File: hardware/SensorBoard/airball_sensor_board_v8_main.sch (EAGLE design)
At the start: 56 parts, among them IC1 CP2102, J2 USB Female Type C Connector, T1 BC846, T2 BC846, U1 BQ24075, U2 BQ27441-G1, U3 BMP388, U4 ESP-WROOM-32, U7 SP0503BAHT

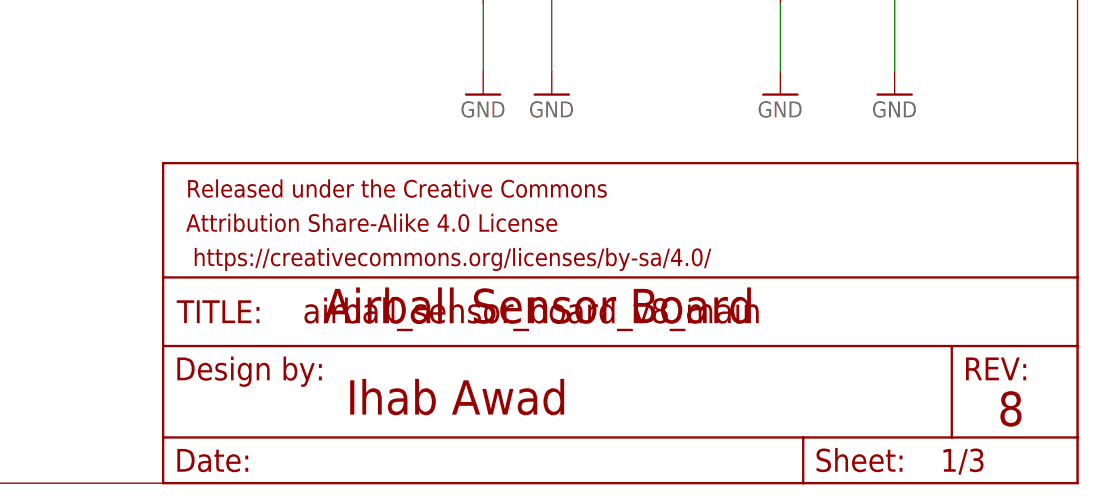
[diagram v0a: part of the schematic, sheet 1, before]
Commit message: More routing and documentation fixes.
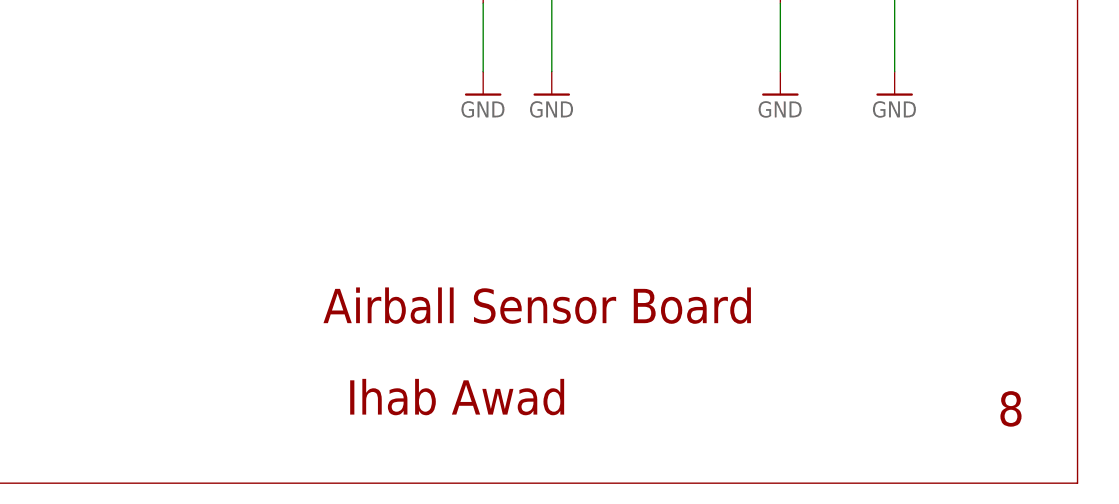
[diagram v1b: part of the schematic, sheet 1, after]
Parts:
- removed FRAME1, FRAME2: FRAME-LETTER, SparkFun-Aesthetics:FRAME-LETTER
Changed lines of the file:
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@@
 <part name="R19" library="SparkFun-Resistors" deviceset="10KOHM-1/10W-1%(0603)" device="0603" value="750"/>
 <part name="GND32" library="SparkFun-PowerSymbols" deviceset="GND" device=""/>
-<part name="FRAME1" library="SparkFun-Aesthetics" deviceset="FRAME-LETTER" device=""/>
-<part name="FRAME2" library="SparkFun-Aesthetics" deviceset="FRAME-LETTER" device=""/>
 </parts>
 <sheets>
@@
 <attribute name="VALUE" x="231.14" y="114.3" size="1.778" layer="96"/>
 </instance>
-<instance part="FRAME2" gate="V" x="149.86" y="0" smashed="yes"/>
 </instances>
 <busses>
@@
 <attribute name="VALUE" x="101.6" y="63.5" size="1.778" layer="96"/>
 </instance>
-<instance part="FRAME1" gate="V" x="152.4" y="0" smashed="yes"/>
 </instances>
 <busses>
